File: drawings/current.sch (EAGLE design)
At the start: 7 parts, among them U1 INA296A5, U2 THS4532IPW

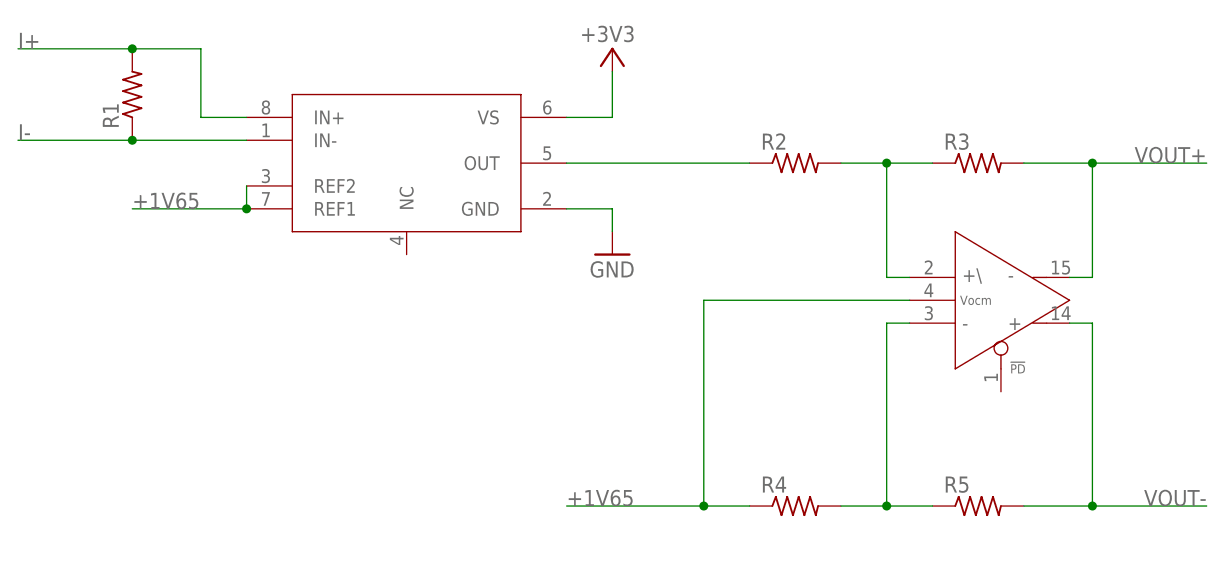
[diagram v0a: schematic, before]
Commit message: Updated drawings of voltage and current circuits
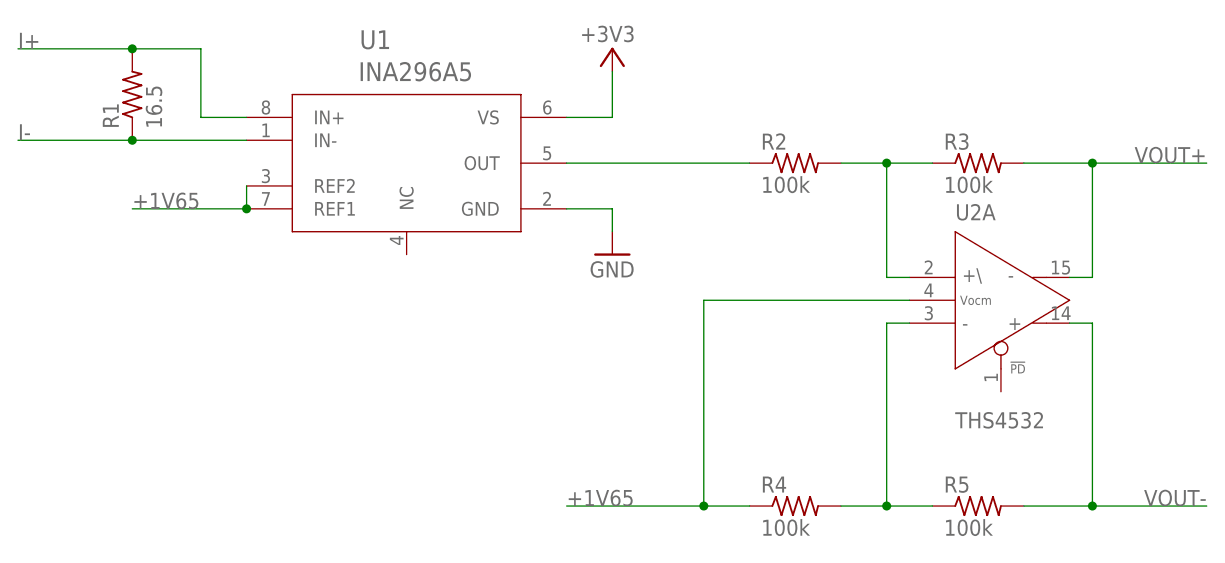
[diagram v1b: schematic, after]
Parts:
- R1: value (none) -> 16.5
- R2, R3, R4, R5: value (none) -> 100k
- U2: value THS4532IPW -> THS4532; device Soil Power Sensor:THS4532IPW -> Soil Power Sensor:THS4532
